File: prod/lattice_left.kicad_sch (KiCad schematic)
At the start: 48 parts

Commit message: matrix finished
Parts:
- added J1, J2: USB_C_Receptacle, Connector_USB:USB_C_Receptacle_HRO_TYPE-C-31-M-12, symbol Connector:USB_C_Receptacle
- added U1: RP2040, Package_DFN_QFN:QFN-56-1EP_7x7mm_P0.4mm_EP3.2x3.2mm, symbol MCU_RaspberryPi:RP2040
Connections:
- new net: J2.A1 (GND), J2.A12 (GND), J2.B1 (GND), J2.B12 (GND)
- new net: J2.A4 (VBUS), J2.A9 (VBUS), J2.B4 (VBUS), J2.B9 (VBUS)
- new net: U1.1 (IOVDD), U1.10 (IOVDD), U1.22 (IOVDD), U1.33 (IOVDD), U1.42 (IOVDD), U1.49 (IOVDD)
- new net: U1.23 (DVDD), U1.50 (DVDD)
- new net: J1.A1 (GND), J1.A12 (GND), J1.B1 (GND), J1.B12 (GND)
- new net: J1.A4 (VBUS), J1.A9 (VBUS), J1.B4 (VBUS), J1.B9 (VBUS)
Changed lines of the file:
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@@
+    )
+  )
+  (symbol (lib_id "Connector:USB_C_Receptacle") (at 83.82 50.8 0) (unit 1)
+    (in_bom yes) (on_board yes) (dnp no) (fields_autoplaced)
+    (property "Reference" "J2" (at 83.82 17.78 0)
+      (effects (font (size 1.27 1.27)))
+    )
+    (property "Value" "USB_C_Receptacle" (at 83.82 20.32 0)
+      (effects (font (size 1.27 1.27)))
+    )
+    (property "Footprint" "Connector_USB:USB_C_Receptacle_HRO_TYPE-C-31-M-12" (at 87.63 50.8 0)
+      (effects (font (size 1.27 1.27)) hide)
+    )
+    (property "Datasheet" "https://www.usb.org/sites/default/files/documents/usb_type-c.zip" (at 87.63 50.8 0)
+      (effects (font (size 1.27 1.27)) hide)
+    )
+    (pin "A9")
+    (pin "B5")
+    (pin "A4")
+    (pin "A3")
+    (pin "A6")
+    (pin "B1")
+    (pin "A1")
+    (pin "A8")
+    (pin "B10")
+    (pin "B11")
+    (pin "A10")
+    (pin "A7")
+    (pin "B12")
+    (pin "B2")
+    (pin "A11")
+    (pin "B4")
+    (pin "B3")
+    (pin "B7")
+    (pin "B6")
+    (pin "A12")
+    (pin "A5")
+    (pin "B8")
+    (pin "A2")
+    (pin "B9")
+    (pin "S1")
+    (instances
+      (project "lattice_left"
+        (path "/7175bad1-6d67-4925-85bf-3e5286dbd285"
+          (reference "J2") (unit 1)
+        )
+      )
     )
   )
@@
     )
   )
+  (symbol (lib_id "MCU_RaspberryPi:RP2040") (at 88.9 143.51 90) (unit 1)
+    (in_bom yes) (on_board yes) (dnp no) (fields_autoplaced)
+    (property "Reference" "U1" (at 135.89 141.2941 90)
+      (effects (font (size 1.27 1.27)))
+    )
+    (property "Value" "RP2040" (at 135.89 143.8341 90)
+      (effects (font (size 1.27 1.27)))
+    )
+    (property "Footprint" "Package_DFN_QFN:QFN-56-1EP_7x7mm_P0.4mm_EP3.2x3.2mm" (at 88.9 143.51 0)
+      (effects (font (size 1.27 1.27)) hide)
+    )
+    (property "Datasheet" "https://datasheets.raspberrypi.com/rp2040/rp2040-datasheet.pdf" (at 88.9 143.51 0)
+      (effects (font (size 1.27 1.27)) hide)
+    )
+    (pin "44")
+    (pin "7")
+    (pin "39")
+    (pin "56")
+    (pin "50")
+    (pin "54")
+    (pin "55")
+    (pin "57")
+    (pin "37")
+    (pin "43")
+    (pin "8")
+    (pin "49")
+    (pin "52")
+    (pin "5")
+    (pin "48")
+    (pin "46")
+    (pin "51")
+    (pin "47")
+    (pin "41")
+    (pin "38")
+    (pin "45")
+    (pin "40")
+    (pin "9")
+    (pin "53")
+    (pin "4")
+    (pin "42")
+    (pin "6")
+    (pin "16")
+    (pin "3")
+    (pin "17")
+    (pin "36")
+    (pin "22")
+    (pin "30")
+    (pin "32")
+    (pin "34")
+    (pin "21")
+    (pin "19")
+    (pin "13")
+    (pin "15")
+    (pin "23")
+    (pin "28")
+    (pin "35")
+    (pin "20")
+    (pin "27")
+    (pin "14")
+    (pin "31")
+    (pin "2")
+    (pin "18")
+    (pin "33")
+    (pin "26")
+    (pin "24")
+    (pin "29")
+    (pin "25")
+    (pin "1")
+    (pin "12")
+    (pin "10")
+    (pin "11")
+    (instances
+      (project "lattice_left"
+        (path "/7175bad1-6d67-4925-85bf-3e5286dbd285"
+          (reference "U1") (unit 1)
+        )
+      )
+    )
+  )
   (symbol (lib_id "marbastlib-mx:MX_SW_HS") (at 228.6 60.96 180) (unit 1)
     (in_bom yes) (on_board yes) (dnp no) (fields_autoplaced)
@@
         )
       )
+    )
+  )
+  (symbol (lib_id "Connector:USB_C_Receptacle") (at 30.48 50.8 0) (unit 1)
+    (in_bom yes) (on_board yes) (dnp no) (fields_autoplaced)
+    (property "Reference" "J1" (at 30.48 17.78 0)
+      (effects (font (size 1.27 1.27)))
+    )
+    (property "Value" "USB_C_Receptacle" (at 30.48 20.32 0)
+      (effects (font (size 1.27 1.27)))
+    )
+    (property "Footprint" "Connector_USB:USB_C_Receptacle_HRO_TYPE-C-31-M-12" (at 34.29 50.8 0)
+      (effects (font (size 1.27 1.27)) hide)
+    )
+    (property "Datasheet" "https://www.usb.org/sites/default/files/documents/usb_type-c.zip" (at 34.29 50.8 0)
+      (effects (font (size 1.27 1.27)) hide)
+    )
+    (pin "A9")
+    (pin "B5")
+    (pin "A4")
+    (pin "A3")
+    (pin "A6")
+    (pin "B1")
+    (pin "A1")
+    (pin "A8")
+    (pin "B10")
+    (pin "B11")
+    (pin "A10")
+    (pin "A7")
+    (pin "B12")
+    (pin "B2")
+    (pin "A11")
+    (pin "B4")
+    (pin "B3")
+    (pin "B7")
+    (pin "B6")
+    (pin "A12")
+    (pin "A5")
+    (pin "B8")
+    (pin "A2")
+    (pin "B9")
+    (pin "S1")
+    (instances
+      (project "lattice_left"
+        (path "/7175bad1-6d67-4925-85bf-3e5286dbd285"
+          (reference "J1") (unit 1)
+        )
+      )

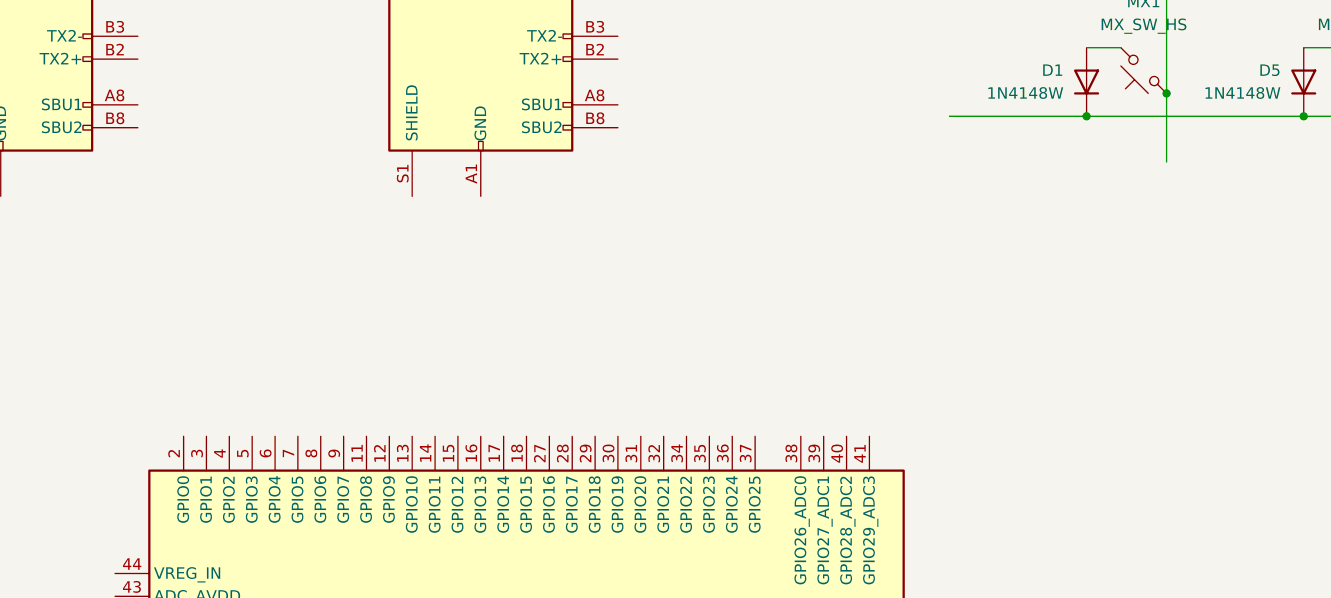
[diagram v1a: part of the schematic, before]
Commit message: silkscreen text
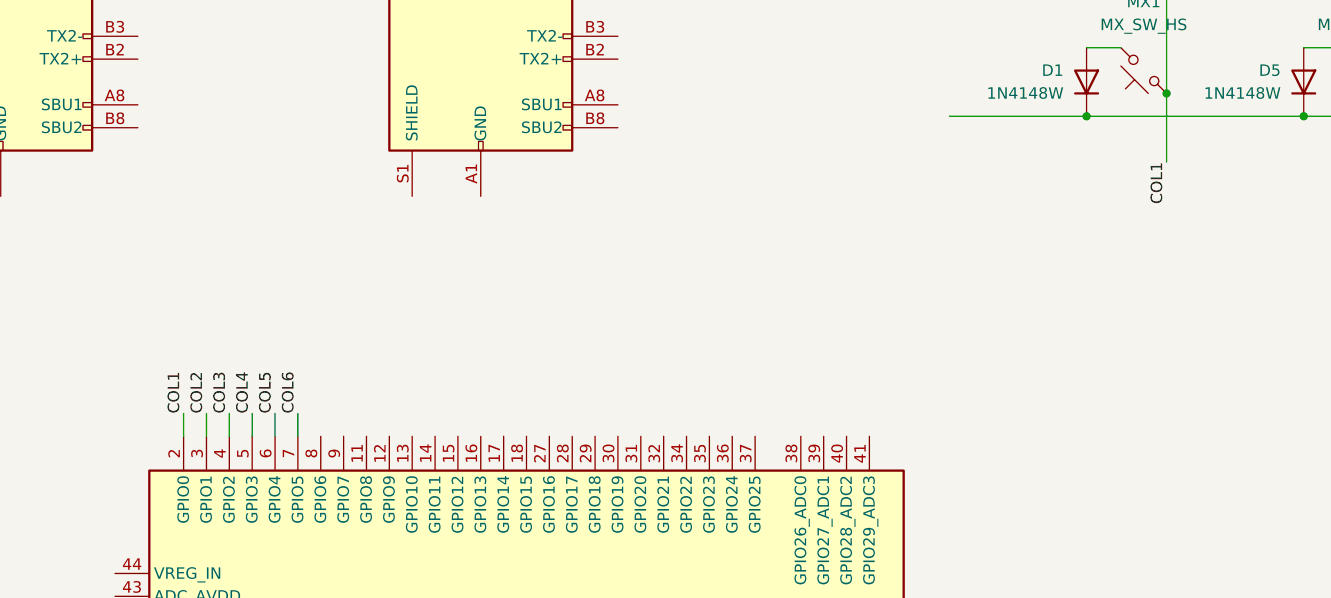
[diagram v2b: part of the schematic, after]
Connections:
- net COL1: now reaches MX1.1, MX2.1, MX3.1, MX4.1
- net COL1: now also U1.2 (GPIO0)
- net COL2: now reaches U1.3 (GPIO1)
- net COL3: now reaches U1.4 (GPIO2)
- net COL4: now reaches U1.5 (GPIO3)
- net COL5: now reaches U1.6 (GPIO4)
- net COL6: now reaches U1.7 (GPIO5)
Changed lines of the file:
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@@
+    (stroke (width 0) (type default))
+  )
+  (wire (pts (xy 58.42 115.57) (xy 58.42 118.11))
     (stroke (width 0) (type default))
   )
@@
     (stroke (width 0) (type default))
   )
+  (wire (pts (xy 53.34 115.57) (xy 53.34 118.11))
+    (stroke (width 0) (type default))
+  )
   (wire (pts (xy 269.24 74.93) (xy 273.05 74.93))
     (stroke (width 0) (type default))
@@
     (stroke (width 0) (type default))
   )
+  (wire (pts (xy 50.8 115.57) (xy 50.8 118.11))
+    (stroke (width 0) (type default))
+  )
   (wire (pts (xy 175.26 82.55) (xy 198.12 82.55))
     (stroke (width 0) (type default))
@@
     (stroke (width 0) (type default))
   )
+  (wire (pts (xy 60.96 115.57) (xy 60.96 118.11))
+    (stroke (width 0) (type default))
+  )
   (wire (pts (xy 222.25 49.53) (xy 246.38 49.53))
     (stroke (width 0) (type default))
@@
     (stroke (width 0) (type default))
   )
+  (wire (pts (xy 63.5 115.57) (xy 63.5 118.11))
+    (stroke (width 0) (type default))
+  )
   (wire (pts (xy 222.25 41.91) (xy 226.06 41.91))
     (stroke (width 0) (type default))
@@
     (stroke (width 0) (type default))
   )
+  (wire (pts (xy 55.88 115.57) (xy 55.88 118.11))
+    (stroke (width 0) (type default))
+  )
   (wire (pts (xy 184.15 46.99) (xy 184.15 63.5))
     (stroke (width 0) (type default))
   )
-  (netclass_flag "" (length 2.54) (shape round) (at 184.15 87.63 180) (fields_autoplaced)
+  (label "COL1" (at 50.8 115.57 90) (fields_autoplaced)
+    (effects (font (size 1.27 1.27)) (justify left bottom))
+    (property "Netclass" "COL1" (at 52.07 115.57 90)
+      (effects (font (size 1.27 1.27) italic) (justify left) hide)
+    )
+  )
+  (label "COL2" (at 53.34 115.57 90) (fields_autoplaced)
+    (effects (font (size 1.27 1.27)) (justify left bottom))
+    (property "Netclass" "COL2" (at 54.61 115.57 90)
+      (effects (font (size 1.27 1.27) italic) (justify left) hide)
+    )
+  )
+  (label "COL4" (at 58.42 115.57 90) (fields_autoplaced)
+    (effects (font (size 1.27 1.27)) (justify left bottom))
+    (property "Netclass" "COL4" (at 59.69 115.57 90)
+      (effects (font (size 1.27 1.27) italic) (justify left) hide)
+    )
+  )
+  (label "COL6" (at 63.5 115.57 90) (fields_autoplaced)
+    (effects (font (size 1.27 1.27)) (justify left bottom))
+    (property "Netclass" "COL6" (at 64.77 115.57 90)
+      (effects (font (size 1.27 1.27) italic) (justify left) hide)
+    )
+  )
+  (label "COL1" (at 160.02 87.63 270) (fields_autoplaced)
     (effects (font (size 1.27 1.27)) (justify right bottom))
-    (property "Netclass" "COL2" (at 184.8485 90.17 0)
-      (effects (font (size 1.27 1.27) italic) (justify left))
+    (property "Netclass" "COL1" (at 161.29 87.63 90)
+      (effects (font (size 1.27 1.27) italic) (justify right) hide)
+    )
+  )
+  (label "COL3" (at 55.88 115.57 90) (fields_autoplaced)
+    (effects (font (size 1.27 1.27)) (justify left bottom))
+    (property "Netclass" "COL3" (at 57.15 115.57 90)
+      (effects (font (size 1.27 1.27) italic) (justify left) hide)
+    )
+  )
+  (label "COL5" (at 60.96 115.57 90) (fields_autoplaced)
+    (effects (font (size 1.27 1.27)) (justify left bottom))
+    (property "Netclass" "COL5" (at 62.23 115.57 90)
+      (effects (font (size 1.27 1.27) italic) (justify left) hide)
     )
   )
@@
     )
   )
-  (netclass_flag "" (length 2.54) (shape round) (at 160.02 87.63 180) (fields_autoplaced)
-    (effects (font (size 1.27 1.27)) (justify right bottom))
-    (property "Netclass" "COL1" (at 160.7185 90.17 0)
-      (effects (font (size 1.27 1.27) italic) (justify left))
-    )
-  )
   (netclass_flag "" (length 2.54) (shape round) (at 135.89 49.53 90) (fields_autoplaced)
     (effects (font (size 1.27 1.27)) (justify left bottom))
@@
       (effects (font (size 1.27 1.27) italic) (justify left))
     )
-  )
-  (netclass_flag "" (length 2.54) (shape round) (at 207.01 87.63 180) (fields_autoplaced)
-    (effects (font (size 1.27 1.27)) (justify right bottom))
-    (property "Netclass" "COL3" (at 207.7085 90.17 0)
-      (effects (font (size 1.27 1.27) italic) (justify left))
-    )

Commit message: placing major rp2040 components
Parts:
- added F1: Polyfuse_Small, Fuse:Fuse_0603_1608Metric, symbol Device:Polyfuse_Small
- added R1, R2: R_Small, symbol Device:R_Small
- added SYM1: Logo_Open_Hardware_Small, Symbol:OSHW-Logo_5.7x6mm_SilkScreen, symbol Graphic:Logo_Open_Hardware_Small
- added U2: W25Q128JVS, Package_SO:SOIC-8_5.23x5.23mm_P1.27mm, symbol Memory_Flash:W25Q128JVS
- added U3: USBLC6-2SC6, Package_TO_SOT_SMD:SOT-23-6, symbol Power_Protection:USBLC6-2SC6
- added U4: XC6206PxxxMR, Package_TO_SOT_SMD:SOT-23-3, symbol Regulator_Linear:XC6206PxxxMR
- added Y1: Crystal_GND24_Small, Crystal:Crystal_SMD_3225-4Pin_3.2x2.5mm, symbol Device:Crystal_GND24_Small
- MX1, MX10, MX11, MX12, MX13, MX14, MX15, MX16, MX17, MX18, MX19, MX2, MX20, MX21, MX22, MX23, MX24, MX3, MX4, MX5, MX6, MX7, MX8, MX9: footprint marbastlib-mx:SW_MX_HS_1u -> lattice:SW_MX_HS_1u
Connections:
- net COL2: now also MX5.1, MX6.1, MX7.1, MX8.1
- net COL3: now also MX10.1, MX11.1, MX12.1, MX9.1
- net COL4: now also MX13.1, MX14.1, MX15.1, MX16.1
- net COL5: now also MX17.1, MX18.1, MX19.1, MX20.1
- net COL6: now also MX21.1, MX22.1, MX23.1, MX24.1
- net ROW3: now reaches D10.1 (K), D14.1 (K), D18.1 (K), D2.1 (K), D22.1 (K), D6.1 (K)
- net ROW3: now also U1.11 (GPIO8)
- net ROW1: now reaches D12.1 (K), D16.1 (K), D20.1 (K), D24.1 (K), D4.1 (K), D8.1 (K)
- net ROW1: now also U1.8 (GPIO6)
- net ROW2: now reaches D11.1 (K), D15.1 (K), D19.1 (K), D23.1 (K), D3.1 (K), D7.1 (K)
- net ROW2: now also U1.9 (GPIO7)
- net ROW4: now reaches D1.1 (K), D13.1 (K), D17.1 (K), D21.1 (K), D5.1 (K), D9.1 (K)
- net ROW4: now also U1.12 (GPIO9)
- net GND: now reaches J2.A1 (GND), J2.A12 (GND), J2.B1 (GND), J2.B12 (GND)
- net GND: now also J1.A1 (GND), J1.A12 (GND), J1.B1 (GND), J1.B12 (GND), U1.57 (GND), R1.2, R2.2
- net at J2.A6 (D+): now also J2.B6 (D+)
- net at J2.A7 (D-): now also J2.B7 (D-)
- net +3V3: now reaches J1.A4 (VBUS), J1.A9 (VBUS), J1.B4 (VBUS), J1.B9 (VBUS)
- net +3V3: now also F1.1
- net CC1: now reaches J1.A5 (CC1)
- net CC1: now also R1.1
- net at J1.A6 (D+): now also J1.B6 (D+)
- net at J1.A7 (D-): now also J1.B7 (D-)
- net at J1.B10 (RX1-): now also J1.B11 (RX1+)
- net CC2: now reaches J1.B5 (CC2)
- net CC2: now also R2.1
- new net +5V: F1.2
- no-connect marks 0 -> 6
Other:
- moved on the sheet: U1

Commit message: more work on schematic
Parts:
- added C1: 100nf, symbol Device:C_Small
- added R3, R4: 27R, symbol Device:R_Small
- added R5, R6: 1k, symbol Device:R_Small
- F1: value Polyfuse_Small -> 500mA
- R1, R2: value R_Small -> 5k1; footprint (none) -> Resistor_SMD:R_0603_1608Metric
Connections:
- net +3V3: now also U1.1 (IOVDD), U1.10 (IOVDD), U1.22 (IOVDD), U1.33 (IOVDD), U1.42 (IOVDD), U1.43 (ADC_AVDD), U1.44 (VREG_IN), U1.48 (USB_VDD), U1.49 (IOVDD), U2.8 (VCC), C1.2, R5.1; no longer F1.1, J1.A4 (VBUS), J1.A9 (VBUS), J1.B4 (VBUS), J1.B9 (VBUS)
- net +5V: now also U3.5 (VBUS)
- net GND: now also U1.19 (TESTEN), U2.4 (GND), U3.2 (GND), U4.1 (GND), C1.1
- net at J2.A10 (RX2-): now also J2.B10 (RX1-)
- net at J2.A11 (RX2+): now also J2.B11 (RX1+)
- net at J2.A2 (TX1+): now also J2.B2 (TX2+)
- net at J2.A3 (TX1-): now also J2.B3 (TX2-)
- net at J2.A6 (D+): no longer J2.B6 (D+)
- net at J2.A7 (D-): no longer J2.B7 (D-)
- net D_P: now reaches U3.1 (I/O1)
- net D_P: now also R3.2
- net D_N: now reaches U3.3 (I/O2)
- net D_N: now also R4.2
- net D_USB_N: now reaches U3.4 (I/O2)
- net D_USB_N: now also J1.A7 (D-), J1.B7 (D-)
- net D_USB_P: now reaches U3.6 (I/O1)
- net D_USB_P: now also J1.A6 (D+), J1.B6 (D+)
- net SD1: now reaches U2.2 (DO(IO1))
- net SD1: now also U1.55 (QSPI_SD1)
- net SD2: now reaches U2.3 (IO2)
- net SD2: now also U1.54 (QSPI_SD2)
- net SD0: now reaches U2.5 (DI(IO0))
- net SD0: now also U1.53 (QSPI_SD0)
- net QSPI_CLK: now reaches U2.6 (CLK)
- net QSPI_CLK: now also U1.52 (QSPI_SCLK)
- net SD3: now reaches U2.7 (IO3)
- net SD3: now also U1.51 (QSPI_SD3)
- net XTAL_IN: now reaches U1.20 (XIN)
- net XTAL_OUT: now reaches U1.21 (XOUT)
- net +1V1: now reaches U1.23 (DVDD), U1.50 (DVDD)
- net +1V1: now also U1.45 (VREG_VOUT)
- net SWCLK: now reaches U1.24 (SWCLK)
- net SWD: now reaches U1.25 (SWD)
- net RESET: now reaches U1.26 (RUN)
- net RESET: now also R5.2
- net at U1.46 (USB_DM): now also R4.1
- net at U1.47 (USB_DP): now also R3.1
- net CS: now reaches U1.56 (QSPI_SS)
- net at J1.B10 (RX1-): no longer J1.B11 (RX1+)
- net CC1: no longer names the net of J1.A5 (CC1), R1.1
- net CC2: no longer names the net of J1.B5 (CC2), R2.1
- new net VBUS: F1.1, J1.A4 (VBUS), J1.A9 (VBUS), J1.B4 (VBUS), J1.B9 (VBUS)
- no-connect marks 6 -> 18
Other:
- note added: "USB - Host"
- note added: "USB - Peripheral"
- moved on the sheet: J2, U2, U3, U4, Y1
